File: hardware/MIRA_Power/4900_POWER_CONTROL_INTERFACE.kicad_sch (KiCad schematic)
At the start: 5 parts, among them J4901 POWER_CONTROL_2x32_P2.54, J4902 CORE_POWER_SENSE_2x09, U4901 74LVC1G17GV,125

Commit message: Select Samtec inter-board connectors and resolve analog VSS ERC warnings
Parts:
- J4901: value POWER_CONTROL_2x32_P2.54 -> SSW-132-01-S-D; footprint MIRA_RevA:PinHeader_2x32_P2.54mm_Vertical -> MIRA_RevA:Samtec_SSW-132-01-S-D_2x32_P2.54mm_Vertical; symbol MIRA_RevA:POWER_CONTROL_64_POWER_MIRA -> MIRA_RevA:SSW_132_01_S_D_MIRA_POWER; DesignStatus PRELIMINARY: no connector pair or thermal approval -> Selected for parallel stack; PCB placement and thermal qual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; MPN (none) -> SSW-132-01-S-D; Manufacturer (none) -> Samtec; Mate (none) -> HTSW-132-07-S-D; MountSide (none) -> F.Cu; StackGap (none) -> 12.00 mm between facing board surfaces
- J4902: value CORE_POWER_SENSE_2x09 -> SSW-109-01-S-D; footprint MIRA_RevA:PinHeader_2x09_P2.54mm_Vertical -> MIRA_RevA:Samtec_SSW-109-01-S-D_2x09_P2.54mm_Vertical; symbol MIRA_RevA:CORE_POWER_SENSE_2x09 -> MIRA_RevA:SSW_109_01_S_D_MIRA_CORE; DesignStatus PRELIMINARY; pair MPN and contact resistance/thermal rating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 -> Selected for parallel stack; PCB placement and thermal qual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; MPN (none) -> SSW-109-01-S-D; Manufacturer (none) -> Samtec; Mate (none) -> HTSW-109-07-S-D; MountSide (none) -> F.Cu; StackGap (none) -> 12.00 mm between facing board surfaces
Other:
- note added: "12 mm stack: Power sockets F.Cu; Control headers B.Cu. No hot-plug."
- note added: "J4901: SSW-132-01-S-D; mate J400: HTSW-132-07-S-D."
- note added: "J4902 SSW-109-01-S-D <-> J401 HTSW-109-07-S-D."
- note removed: "B03 OPEN: select connector pair, current rating and mechanical stack."
- note removed: "J4902.n <-> J401.n; supplemental CORE power path."
- note removed: "No hot-plug. Voltage-drop / GND / VTT routing checks remain required."
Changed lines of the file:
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@@
 (kicad_sch (version 20260306) (generator "eeschema") (generator_version "10.0") (paper "A3") (title_block (title "MIRA Power-Control interface") (rev "B1") (company "MIRA"))
-(symbol (lib_id "MIRA_RevA:POWER_CONTROL_64_POWER_MIRA") (at 88.9 125.73 0) (unit 1) (in_bom yes) (on_board yes) (dnp no)
+(symbol (lib_id "MIRA_RevA:SSW_132_01_S_D_MIRA_POWER") (at 88.9 125.73 0) (unit 1) (in_bom yes) (on_board yes) (dnp no)
 (property "Reference" "J4901" (at 88.9 76.2 0) (effects (font (size 1.016 1.016))))
-(property "Value" "POWER_CONTROL_2x32_P2.54" (at 88.9 78.74 0) (effects (font (size 1.016 1.016))))
-(property "Footprint" "MIRA_RevA:PinHeader_2x32_P2.54mm_Vertical" (at 88.9 125.73 0) (hide yes) (effects (font (size 1.016 1.016))))
-(property "Datasheet" "" (at 88.9 125.73 0) (hide yes) (effects (font (size 1.016 1.016))))
-(property "Description" "Same-number wiring to Control J400. MPN, mate and footprint approval pending B03." (at 88.9 125.73 0) (hide yes) (effects (font (size 1.016 1.016))))
-(property "MPN" "" (at 88.9 125.73 0) (hide yes) (effects (font (size 1.016 1.016))))
-(property "Manufacturer" "" (at 88.9 125.73 0) (hide yes) (effects (font (size 1.016 1.016))))
-(property "DesignStatus" "PRELIMINARY: no connector pair or thermal approval" (at 88.9 125.73 0) (hide yes) (effects (font (size 1.016 1.016))))
+(property "Value" "SSW-132-01-S-D" (at 88.9 78.74 0) (effects (font (size 1.016 1.016))))
+(property "Footprint" "MIRA_RevA:Samtec_SSW-132-01-S-D_2x32_P2.54mm_Vertical" (at 88.9 125.73 0) (hide yes) (effects (font (size 1.016 1.016))))
+(property "Datasheet" "https://www.samtec.com/products/ssw-132-01-s-d" (at 88.9 125.73 0) (hide yes) (effects (font (size 1.016 1.016))))
+(property "Description" "64-contact, 2.54mm, socket; 30uin gold mating contacts; project pin assignment" (at 88.9 125.73 0) (hide yes) (effects (font (size 1.016 1.016))))
+(property "MPN" "SSW-132-01-S-D" (at 88.9 125.73 0) (hide yes) (effects (font (size 1.016 1.016))))
+(property "Manufacturer" "Samtec" (at 88.9 125.73 0) (hide yes) (effects (font (size 1.016 1.016))))
+(property "DesignStatus" "Selected for parallel stack; PCB placement and thermal qualification pending" (at 88.9 125.73 0) (hide yes) (effects (font (size 1.016 1.016))))
 (pin "1")
 (pin "2")
@@
 (pin "63")
 (pin "64")
-(instances (project "MIRA_Power" (path "/5c3dfbc0-84d7-4846-b0d0-d1c9bc7280bc/dbdc5547-ddd8-4565-b568-f55141960e57" (reference "J4901") (unit 1)))))
+(instances (project "MIRA_Power" (path "/5c3dfbc0-84d7-4846-b0d0-d1c9bc7280bc/dbdc5547-ddd8-4565-b568-f55141960e57" (reference "J4901") (unit 1))))
+(property "Mate" "HTSW-132-07-S-D" (at 88.9 125.73 0) (effects (font (size 1 1)) (hide yes)))
+(property "MountSide" "F.Cu" (at 88.9 125.73 0) (effects (font (size 1 1)) (hide yes)))
+(property "StackGap" "12.00 mm between facing board surfaces" (at 88.9 125.73 0) (effects (font (size 1 1)) (hide yes)))
+)
 (wire (pts (xy 71.12 86.36) (xy 63.5 86.36)) (stroke (width 0) (type default)))
 (global_label "AON" (shape input) (at 63.5 86.36 180) (effects (font (size 1.016 1.016)) (justify right)))
@@
 (text "SYS3V3-domain status outputs: U3301; fault input -> matrix latch clear." (at 35.56 196.85 0) (effects (font (size 1.27 1.27)) (justify left bottom)))
 (text "HOST_ALIVE is status only; HOST_WDI remains the hardware heartbeat." (at 35.56 204.47 0) (effects (font (size 1.27 1.27)) (justify left bottom)))
-(text "B03 OPEN: select connector pair, current rating and mechanical stack." (at 35.56 212.09 0) (effects (font (size 1.27 1.27)) (justify left bottom)))
-(text "No hot-plug. Voltage-drop / GND / VTT routing checks remain required." (at 35.56 219.71 0) (effects (font (size 1.27 1.27)) (justify left bottom)))
+(text "J4901: SSW-132-01-S-D; mate J400: HTSW-132-07-S-D." (at 35.56 212.09 0) (effects (font (size 1.27 1.27)) (justify left bottom)))
+(text "12 mm stack: Power sockets F.Cu; Control headers B.Cu. No hot-plug." (at 35.56 219.71 0) (effects (font (size 1.27 1.27)) (justify left bottom)))
 (embedded_fonts no)
-(symbol (lib_id "MIRA_RevA:CORE_POWER_SENSE_2x09") (at 340.36 101.6 0) (unit 1) (in_bom yes) (on_board yes) (dnp no)(property "Reference" "J4902" (at 340.36 69.85 0) (effects (font (size 1.016 1.016))))(property "Value" "CORE_POWER_SENSE_2x09" (at 340.36 72.39 0) (effects (font (size 1.016 1.016))))(property "Footprint" "MIRA_RevA:PinHeader_2x09_P2.54mm_Vertical" (at 340.36 101.6 0) (effects (font (size 1.016 1.016)) (hide yes)))(property "Description" "8 power contacts, 9 return contacts, 1 positive sense. Mating MPN/current validation pending." (at 340.36 101.6 0) (effects (font (size 1.016 1.016)) (hide yes)))(property "DesignStatus" "PRELIMINARY; pair MPN and contact resistance/thermal rating must be approved" (at 340.36 101.6 0) (effects (font (size 1.016 1.016)) (hide yes)))(pin "1")(pin "2")(pin "3")(pin "4")(pin "5")(pin "6")(pin "7")(pin "8")(pin "9")(pin "10")(pin "11")(pin "12")(pin "13")(pin "14")(pin "15")(pin "16")(pin "17")(pin "18")(instances (project "MIRA_Power" (path "/5c3dfbc0-84d7-4846-b0d0-d1c9bc7280bc/dbdc5547-ddd8-4565-b568-f55141960e57" (reference "J4902") (unit 1)))))
+(symbol (lib_id "MIRA_RevA:SSW_109_01_S_D_MIRA_CORE") (at 340.36 101.6 0) (unit 1) (in_bom yes) (on_board yes) (dnp no)(property "Reference" "J4902" (at 340.36 69.85 0) (effects (font (size 1.016 1.016))))(property "Value" "SSW-109-01-S-D" (at 340.36 72.39 0) (effects (font (size 1.016 1.016))))(property "Footprint" "MIRA_RevA:Samtec_SSW-109-01-S-D_2x09_P2.54mm_Vertical" (at 340.36 101.6 0) (effects (font (size 1.016 1.016)) (hide yes)))(property "Description" "18-contact, 2.54mm, socket; 30uin gold mating contacts; project pin assignment" (at 340.36 101.6 0) (effects (font (size 1.016 1.016)) (hide yes)))(property "DesignStatus" "Selected for parallel stack; PCB placement and thermal qualification pending" (at 340.36 101.6 0) (effects (font (size 1.016 1.016)) (hide yes)))(pin "1")(pin "2")(pin "3")(pin "4")(pin "5")(pin "6")(pin "7")(pin "8")(pin "9")(pin "10")(pin "11")(pin "12")(pin "13")(pin "14")(pin "15")(pin "16")(pin "17")(pin "18")(instances (project "MIRA_Power" (path "/5c3dfbc0-84d7-4846-b0d0-d1c9bc7280bc/dbdc5547-ddd8-4565-b568-f55141960e57" (reference "J4902") (unit 1))))
+(property "Datasheet" "https://www.samtec.com/products/ssw-109-01-s-d" (at 340.36 101.6 0) (effects (font (size 1 1)) (hide yes)))
+(property "MPN" "SSW-109-01-S-D" (at 340.36 101.6 0) (effects (font (size 1 1)) (hide yes)))
+(property "Manufacturer" "Samtec" (at 340.36 101.6 0) (effects (font (size 1 1)) (hide yes)))
+(property "Mate" "HTSW-109-07-S-D" (at 340.36 101.6 0) (effects (font (size 1 1)) (hide yes)))
+(property "MountSide" "F.Cu" (at 340.36 101.6 0) (effects (font (size 1 1)) (hide yes)))
+(property "StackGap" "12.00 mm between facing board surfaces" (at 340.36 101.6 0) (effects (font (size 1 1)) (hide yes)))
+)
 (wire (pts (xy 327.66 81.28) (xy 320.04 81.28)) (stroke (width 0) (type default)))
 (global_label "CORE1V0" (shape input) (at 320.04 81.28 180) (effects (font (size 1.016 1.016)) (justify right)))
@@
 (wire (pts (xy 353.06 121.92) (xy 360.68 121.92)) (stroke (width 0) (type default)))
 (global_label "GND" (shape input) (at 360.68 121.92 0) (effects (font (size 1.016 1.016)) (justify left)))
-(text "J4902.n <-> J401.n; supplemental CORE power path." (at 294.64 160.02 0) (effects (font (size 1.016 1.016)) (justify left bottom)))
+(text "J4902 SSW-109-01-S-D <-> J401 HTSW-109-07-S-D." (at 294.64 160.02 0) (effects (font (size 1.016 1.016)) (justify left bottom)))
 (text "Odd 1..15: CORE; even 2..18: GND; 17: Kelvin sense." (at 294.64 167.64 0) (effects (font (size 1.016 1.016)) (justify left bottom)))
 (text "Pin 17: independent trace to FPGA decoupling on Control." (at 294.64 175.26 0) (effects (font (size 1.016 1.016)) (justify left bottom)))

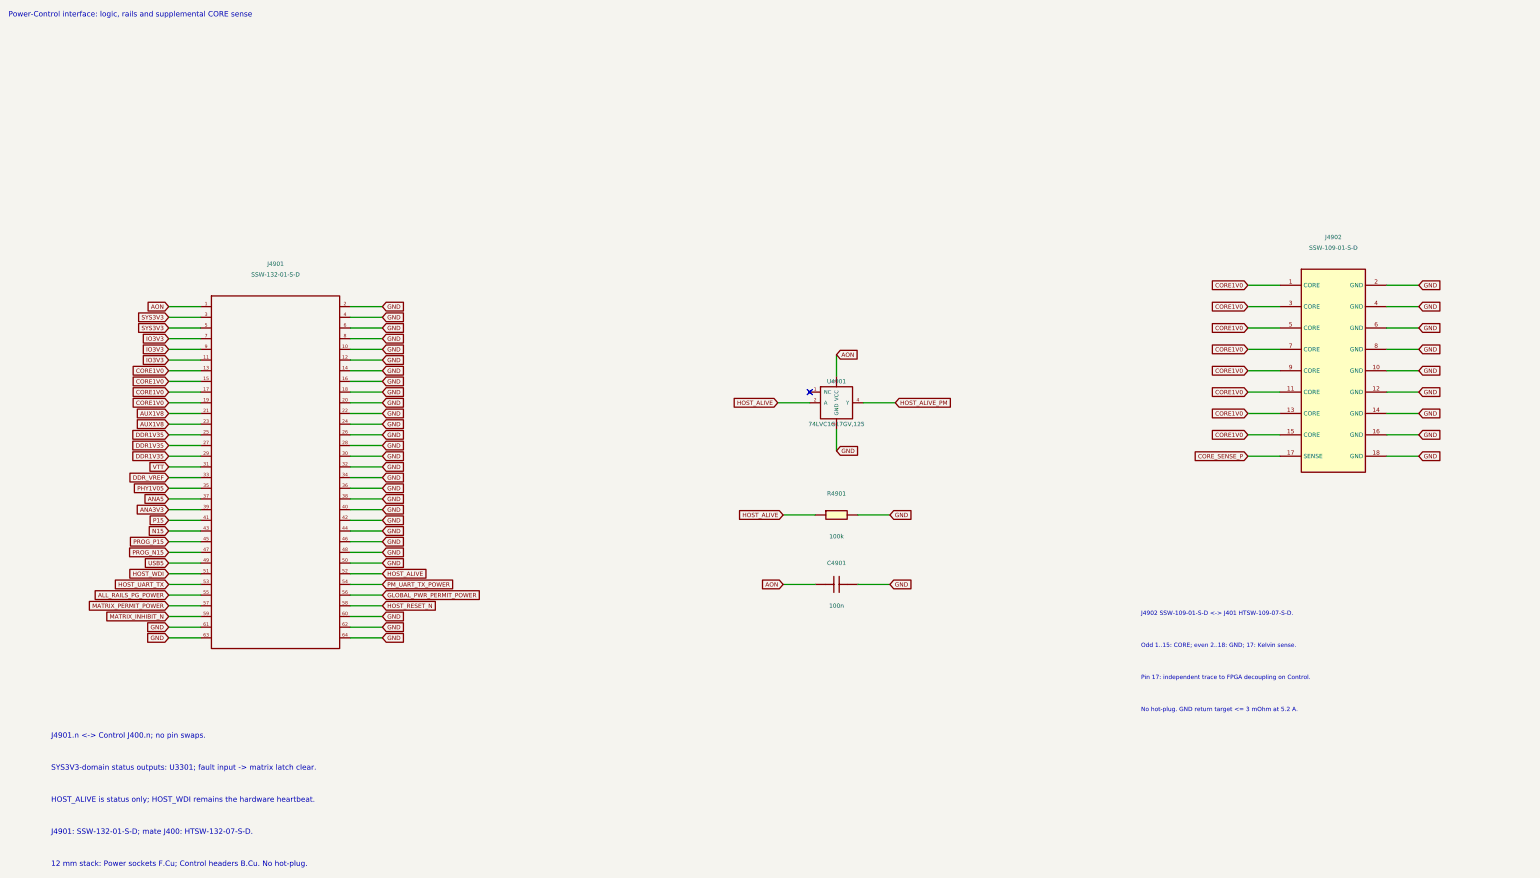
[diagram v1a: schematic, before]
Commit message: Distribute inter-board power across seven load zones and supervision
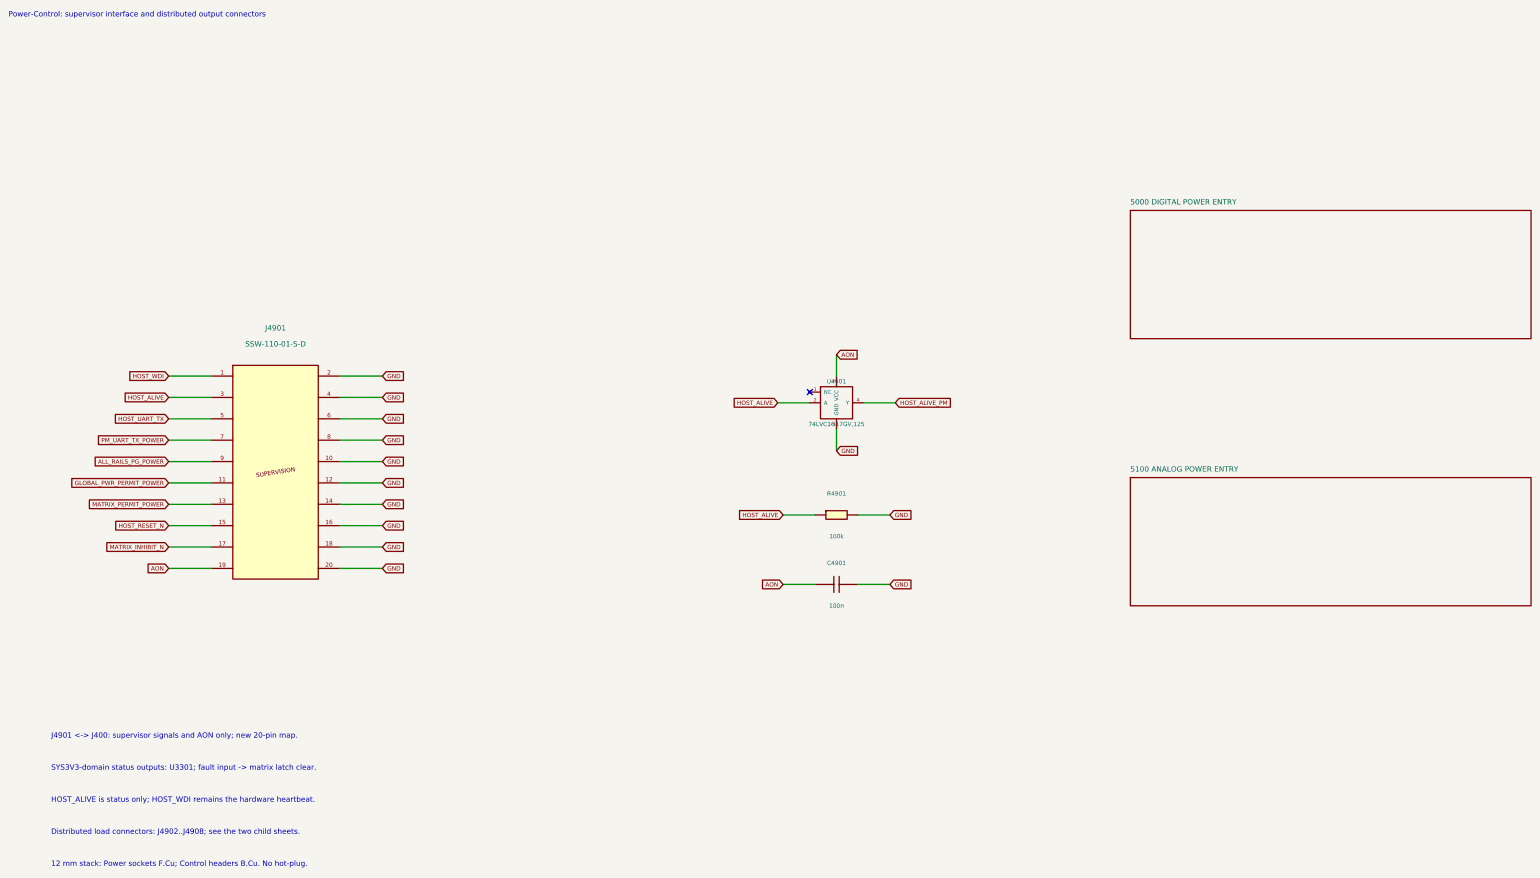
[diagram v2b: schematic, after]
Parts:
- removed J4901: SSW-132-01-S-D, MIRA_RevA:Samtec_SSW-132-01-S-D_2x32_P2.54mm_Vertical, symbol MIRA_RevA:SSW_132_01_S_D_MIRA_POWER
- removed J4902: SSW-109-01-S-D, MIRA_RevA:Samtec_SSW-109-01-S-D_2x09_P2.54mm_Vertical, symbol MIRA_RevA:SSW_109_01_S_D_MIRA_CORE
- added J4901: SSW-110-01-S-D, MIRA_RevA:Samtec_SSW-110-01-S-D_2x10_P2.54mm_Vertical, symbol MIRA_RevA:SSW_110_01_S_D_DIST_SUPERVISION
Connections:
- net ALL_RAILS_PG_POWER: now also J4901.9
- net AON: now also J4901.19
- net GLOBAL_PWR_PERMIT_POWER: now also J4901.11
- net GND: now also J4901.10, J4901.12, J4901.14, J4901.16, J4901.18, J4901.2, J4901.20, J4901.4, J4901.6, J4901.8
- net HOST_ALIVE: now also J4901.3
- net HOST_RESET_N: now also J4901.15
- net HOST_UART_TX: now also J4901.5
- net HOST_WDI: now also J4901.1
- net MATRIX_INHIBIT_N: now also J4901.17
- net MATRIX_PERMIT_POWER: now also J4901.13
- net PM_UART_TX_POWER: now also J4901.7
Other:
- added sheet 5000 DIGITAL POWER ENTRY (5000_DISTRIBUTED_DIGITAL_POWER.kicad_sch)
- added sheet 5100 ANALOG POWER ENTRY (5100_DISTRIBUTED_ANALOG_POWER.kicad_sch)
- note added: "Distributed load connectors: J4902..J4908; see the two child sheets."
- note added: "J4901 <-> J400: supervisor signals and AON only; new 20-pin map."
- note added: "Power-Control: supervisor interface and distributed output connectors"
- note removed: "J4901.n <-> Control J400.n; no pin swaps."
- note removed: "J4901: SSW-132-01-S-D; mate J400: HTSW-132-07-S-D."
- note removed: "J4902 SSW-109-01-S-D <-> J401 HTSW-109-07-S-D."
- note removed: "No hot-plug. GND return target <= 3 mOhm at 5.2 A."
- note removed: "Odd 1..15: CORE; even 2..18: GND; 17: Kelvin sense."
- note removed: "Pin 17: independent trace to FPGA decoupling on Control."
- note removed: "Power-Control interface: logic, rails and supplemental CORE sense"
